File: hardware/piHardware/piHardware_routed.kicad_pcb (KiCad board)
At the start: 2 copper layers, 99.5 x 99.5 mm, 51 parts, among them J1 ST7735, J2 PCM5102A, J3 Battery, SW1 SW_Push, SW2 SW_Push, SW3 SW_Push, SW4 SW_Push, SW5 SW_Push

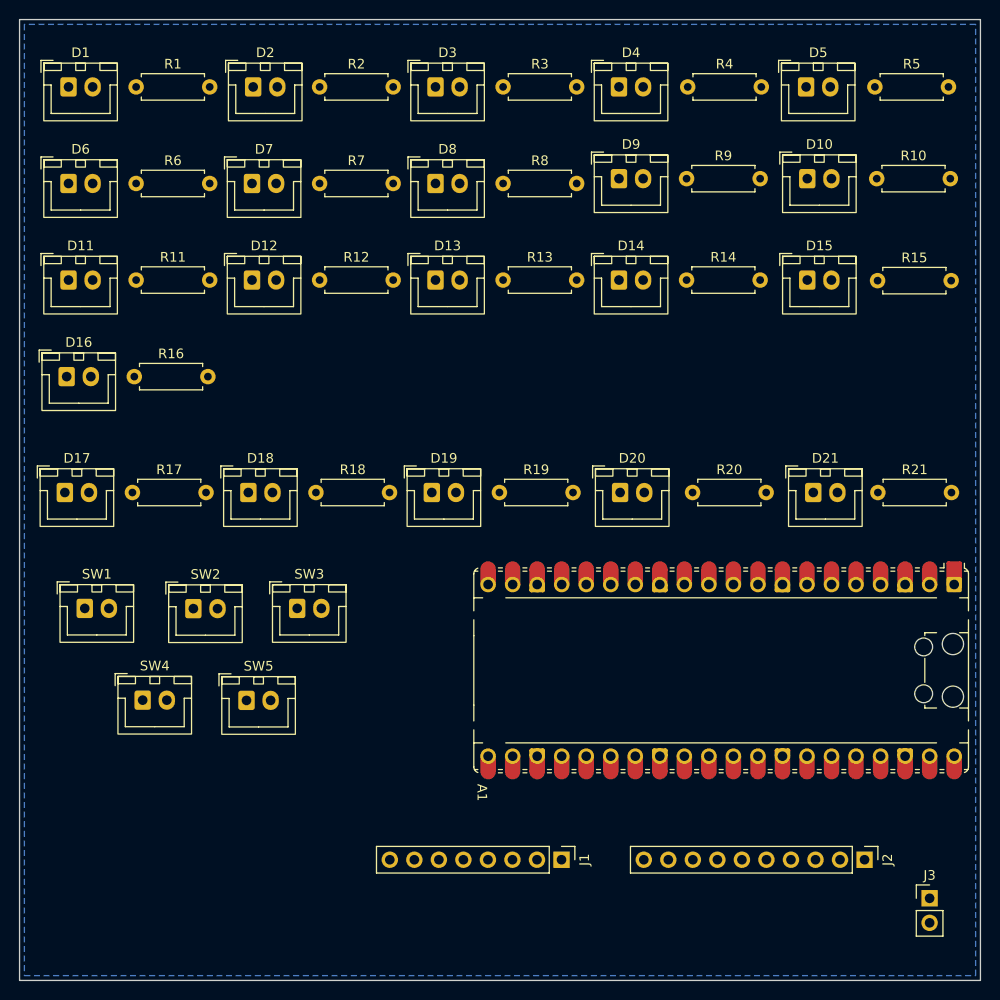
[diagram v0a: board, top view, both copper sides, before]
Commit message: feat:フットプリントと電源ボタンの追加
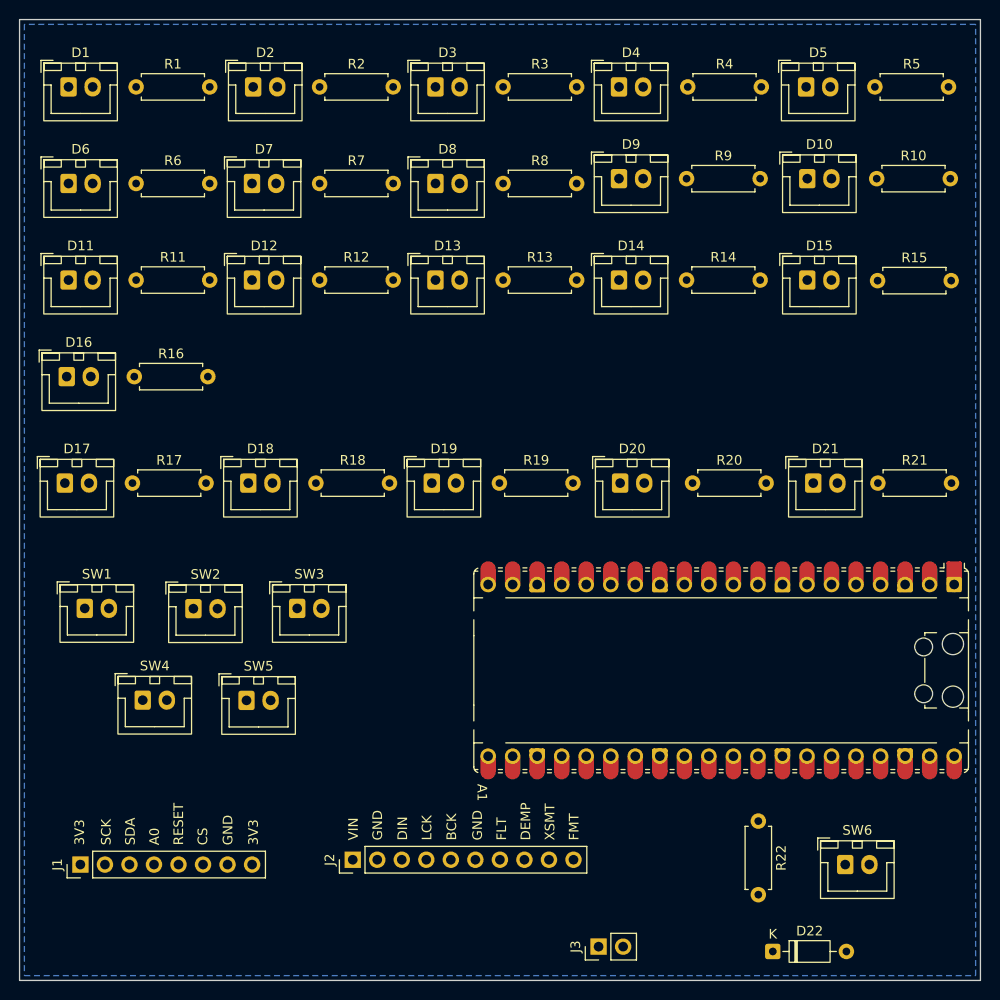
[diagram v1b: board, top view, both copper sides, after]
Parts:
- added D22: 1N914, Diode_THT:D_DO-35_SOD27_P7.62mm_Horizontal, F.Cu at (148.5, 117.0)
- added R22: 1.2k, Resistor_THT:R_Axial_DIN0207_L6.3mm_D2.5mm_P7.62mm_Horizontal, F.Cu at (147.0, 103.5)
- added SW6: SW_Push, Connector_JST:JST_XH_B2B-XH-A_1x02_P2.50mm_Vertical, F.Cu at (156.0, 108.0)
- moved J2 53.0 mm to (105.0, 107.5), turned to 90 degrees
- moved J1 49.8 mm to (76.8, 108.0), turned to 90 degrees
- moved J3 34.6 mm to (130.5, 116.5), turned to 90 degrees
- moved D17 0.97 mm to (75.2, 68.5)
- moved D18 0.97 mm to (94.2, 68.5)
- moved D19 0.97 mm to (113.2, 68.5)
- moved D20 0.97 mm to (132.7, 68.5)
- moved D21 0.97 mm to (152.7, 68.5)
- moved R17 0.97 mm to (82.2, 68.5)
- moved R18 0.97 mm to (101.2, 68.5)
- moved R19 0.97 mm to (120.2, 68.5)
- moved R20 0.97 mm to (140.2, 68.5)
- moved R21 0.97 mm to (159.4, 68.5)
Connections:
- J2 pad 3: /SPK.DIN -> /SPK.BCK
- J2 pad 5: /SPK.BCK -> /SPK.DIN
- J3 pad 1: /battery -> Net-(D22-A)

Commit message: fix:抵抗の削除とスイッチダイオードの変更
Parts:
- removed D22: 1N914, Diode_THT:D_DO-35_SOD27_P7.62mm_Horizontal
- removed R22: 1.2k, Resistor_THT:R_Axial_DIN0207_L6.3mm_D2.5mm_P7.62mm_Horizontal
- added D23: 1N5817, Diode_THT:D_DO-41_SOD81_P10.16mm_Horizontal, F.Cu at (156.5, 114.5)
- SW6: value SW_Push -> SW_SPST
- moved SW6 6.95 mm to (150.0, 104.5)
- moved J3 4.71 mm to (134.7, 114.5)
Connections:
- SW6 pad 1: Net-(R22-Pad2) -> /battery

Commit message: feat:配線の追加
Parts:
- moved J1 66.8 mm to (137.7, 80.5), turned to -90 degrees
- moved J2 25.7 mm to (80.4, 115.0)
- moved D23 19.9 mm to (136.7, 115.5)
- moved J3 18.8 mm to (116.0, 115.5)
- moved SW6 11.0 mm to (145.5, 114.5)
- moved SW4 10.1 mm to (86.8, 100.5)
- moved SW5 10.1 mm to (97.5, 100.5)
- moved A1 8.00 mm to (143.4, 95.9)
- moved SW1 5.88 mm to (81.0, 86.0)
- moved SW2 5.88 mm to (92.2, 86.0)
- moved SW3 5.88 mm to (103.0, 86.0)
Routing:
- net /LED6: track 0.00 -> 160.9 mm
- net /LED1: track 0.00 -> 153.3 mm, vias 0 -> 2
- net /LED7: track 0.00 -> 145.3 mm
- net /LED2: track 0.00 -> 139.4 mm
- net +3V3: track 0.00 -> 135.3 mm
- net /LED8: track 0.00 -> 123.4 mm
- net /LED3: track 0.00 -> 108.3 mm
- net /LED4: track 0.00 -> 94.9 mm
- net /LED9: track 0.00 -> 94.2 mm
- net /LED5: track 0.00 -> 70.5 mm
- net /SPK.BCK: track 0.00 -> 53.8 mm
- net /SPK.DIN: track 0.00 -> 53.7 mm
- net /SPK.LCK: track 0.00 -> 53.2 mm
- net /SW5: track 0.00 -> 51.6 mm
- net /SW4: track 0.00 -> 49.5 mm
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
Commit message: fix:配線とシルクスクリーンの修正
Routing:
- net /LED6: track 160.9 -> 171.6 mm
- net /LED9: track 94.2 -> 104.4 mm
- net /SW3: track 31.9 -> 41.0 mm
- net /LED8: track 123.4 -> 132.3 mm
- net /LED7: track 145.3 -> 153.8 mm
- net /LED3: track 108.3 -> 116.3 mm
- net /SPK.DIN: track 53.7 -> 56.2 mm
- net +3V3: track 135.3 -> 137.8 mm
- net Net-(D23-A): track 11.5 -> 13.6 mm
- net /SW5: track 51.6 -> 52.9 mm
- net /SW4: track 49.5 -> 50.6 mm
- net /LED1: track 153.3 -> 154.4 mm
